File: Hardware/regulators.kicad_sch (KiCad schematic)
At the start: 17 parts, among them J24 DG301-5-0-02P-12-00AH, J25 DG301-5-0-04P-12-00AH, U17 L7812, U19 TLV70033_SOT23-5, U20 TLV73333PDBV

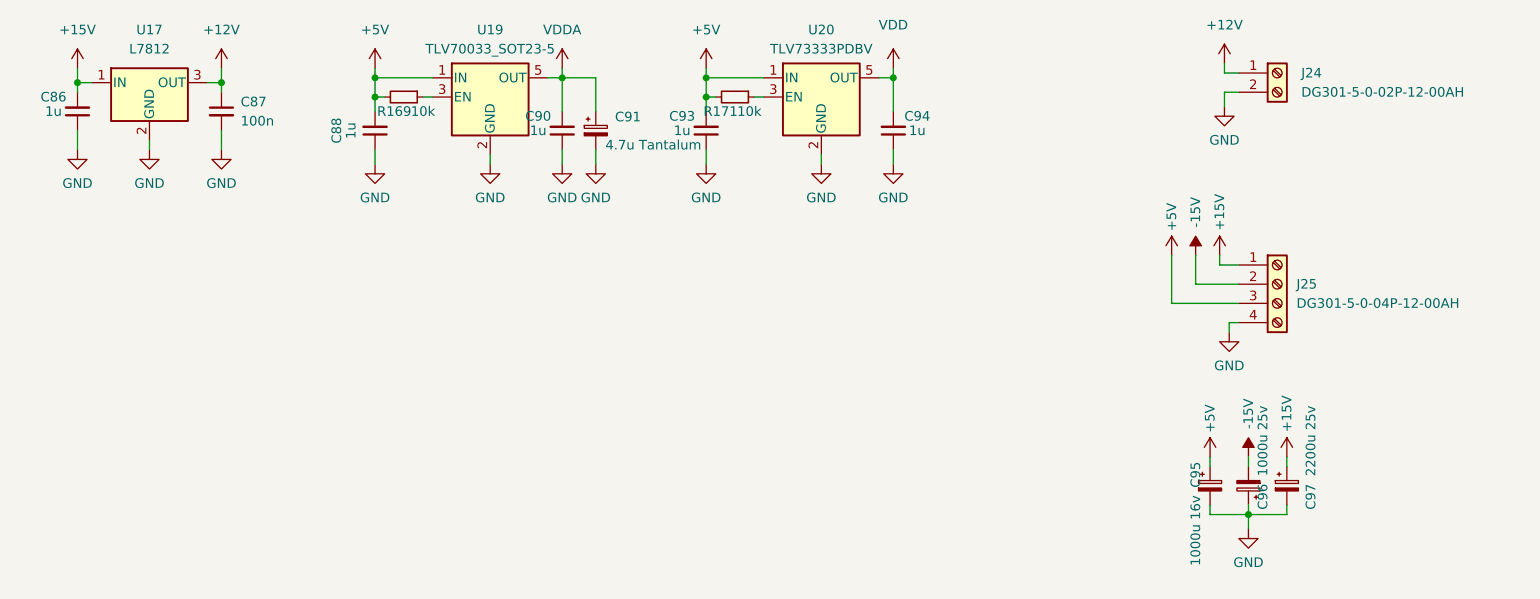
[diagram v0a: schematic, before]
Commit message: Few coonector footprint modifications and silkscreen additions to them.
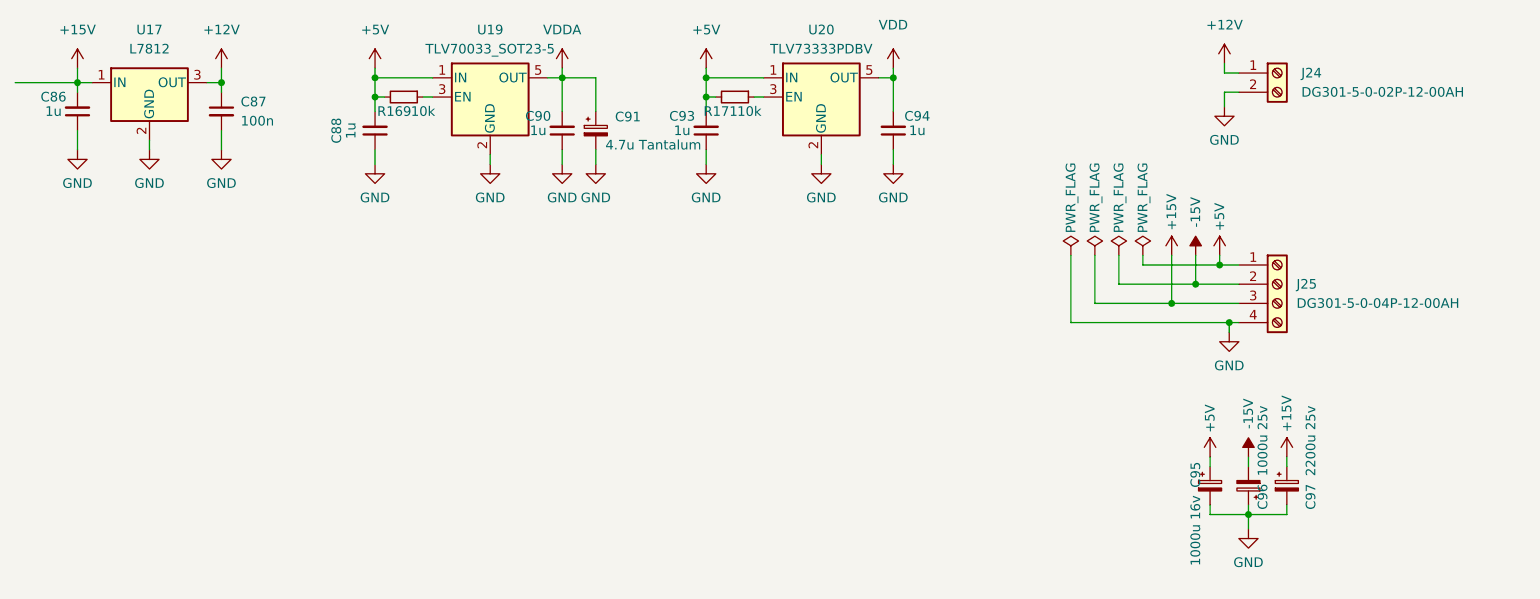
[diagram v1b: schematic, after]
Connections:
- net +15V: now also J25.3 (Pin_3); no longer J25.1 (Pin_1)
- net +5V: now also J25.1 (Pin_1); no longer J25.3 (Pin_3)
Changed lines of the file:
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@@
 (kicad_sch (version 20211123) (generator eeschema)
   (paper "A4")
+  (junction (at 234.95 97.79) (diameter 0) (color 0 0 0 0)
+  )
+  (junction (at 238.125 95.25) (diameter 0) (color 0 0 0 0)
+  )
   (junction (at 245.11 125.73) (diameter 0) (color 0 0 0 0)
   )
+  (junction (at 242.57 100.33) (diameter 0) (color 0 0 0 0)
+  )
   (junction (at 173.355 70.485) (diameter 0) (color 0 0 0 0)
   )
@@
   (junction (at 173.355 67.945) (diameter 0) (color 0 0 0 0)
   )
+  (junction (at 241.3 92.71) (diameter 0) (color 0 0 0 0)
+  )
   (junction (at 109.22 68.58) (diameter 0) (color 0 0 0 0)
   )
@@
     (stroke (width 0) (type default) (color 0 0 0 0))
   )
+  (wire (pts (xy 221.615 91.44) (xy 221.615 100.33))
+    (stroke (width 0) (type default) (color 0 0 0 0))
+  )
   (wire (pts (xy 158.75 72.39) (xy 158.75 67.945))
     (stroke (width 0) (type default) (color 0 0 0 0))
@@
     (stroke (width 0) (type default) (color 0 0 0 0))
   )
+  (wire (pts (xy 81.915 68.58) (xy 90.17 68.58))
+    (stroke (width 0) (type default) (color 0 0 0 0))
+  )
   (wire (pts (xy 173.355 77.47) (xy 173.355 79.375))
     (stroke (width 0) (type default) (color 0 0 0 0))
@@
     (stroke (width 0) (type default) (color 0 0 0 0))
   )
+  (wire (pts (xy 221.615 100.33) (xy 242.57 100.33))
+    (stroke (width 0) (type default) (color 0 0 0 0))
+  )
   (wire (pts (xy 245.11 118.11) (xy 245.11 119.38))
     (stroke (width 0) (type default) (color 0 0 0 0))
@@
     (stroke (width 0) (type default) (color 0 0 0 0))
   )
+  (wire (pts (xy 227.965 91.44) (xy 227.965 95.25))
+    (stroke (width 0) (type default) (color 0 0 0 0))
+  )
   (wire (pts (xy 241.3 92.71) (xy 243.84 92.71))
     (stroke (width 0) (type default) (color 0 0 0 0))
@@
     (stroke (width 0) (type default) (color 0 0 0 0))
   )
+  (wire (pts (xy 224.79 97.79) (xy 234.95 97.79))
+    (stroke (width 0) (type default) (color 0 0 0 0))
+  )
   (wire (pts (xy 109.22 68.58) (xy 109.22 66.675))
     (stroke (width 0) (type default) (color 0 0 0 0))
@@
     (stroke (width 0) (type default) (color 0 0 0 0))
   )
+  (wire (pts (xy 231.14 91.44) (xy 231.14 92.71))
+    (stroke (width 0) (type default) (color 0 0 0 0))
+  )
+  (wire (pts (xy 224.79 91.44) (xy 224.79 97.79))
+    (stroke (width 0) (type default) (color 0 0 0 0))
+  )
   (wire (pts (xy 245.11 125.73) (xy 250.19 125.73))
     (stroke (width 0) (type default) (color 0 0 0 0))
@@
     (stroke (width 0) (type default) (color 0 0 0 0))
   )
+  (wire (pts (xy 231.14 92.71) (xy 241.3 92.71))
+    (stroke (width 0) (type default) (color 0 0 0 0))
+  )
   (wire (pts (xy 241.935 69.85) (xy 241.935 71.755))
     (stroke (width 0) (type default) (color 0 0 0 0))
@@
   )
   (wire (pts (xy 250.19 125.73) (xy 250.19 124.46))
+    (stroke (width 0) (type default) (color 0 0 0 0))
+  )
+  (wire (pts (xy 227.965 95.25) (xy 238.125 95.25))
     (stroke (width 0) (type default) (color 0 0 0 0))
   )
@@
     (pin "2")
   )
-  (symbol (lib_id "power:+15V") (at 241.3 91.44 0) (unit 1)
-    (in_bom yes) (on_board yes)
-    (property "Reference" "#PWR0175" (id 0) (at 241.3 95.25 0)
-      (effects (font (size 1.27 1.27)) hide)
-    )
-    (property "Value" "+15V" (id 1) (at 241.3 85.725 90))
-    (property "Footprint" "" (id 2) (at 241.3 91.44 0)
-      (effects (font (size 1.27 1.27)) hide)
-    )
-    (property "Datasheet" "" (id 3) (at 241.3 91.44 0)
+  (symbol (lib_id "power:PWR_FLAG") (at 224.79 91.44 0) (unit 1)
+    (in_bom yes) (on_board yes)
+    (property "Reference" "#FLG0104" (id 0) (at 224.79 89.535 0)
+      (effects (font (size 1.27 1.27)) hide)
+    )
+    (property "Value" "PWR_FLAG" (id 1) (at 224.79 83.82 90))
+    (property "Footprint" "" (id 2) (at 224.79 91.44 0)
+      (effects (font (size 1.27 1.27)) hide)
+    )
+    (property "Datasheet" "~" (id 3) (at 224.79 91.44 0)
+      (effects (font (size 1.27 1.27)) hide)
+    )
+    (pin "1")
+  )
+  (symbol (lib_id "power:+15V") (at 234.95 91.44 0) (unit 1)
+    (in_bom yes) (on_board yes)
+    (property "Reference" "#PWR0175" (id 0) (at 234.95 95.25 0)
+      (effects (font (size 1.27 1.27)) hide)
+    )
+    (property "Value" "+15V" (id 1) (at 234.95 85.725 90))
+    (property "Footprint" "" (id 2) (at 234.95 91.44 0)
+      (effects (font (size 1.27 1.27)) hide)
+    )
+    (property "Datasheet" "" (id 3) (at 234.95 91.44 0)
       (effects (font (size 1.27 1.27)) hide)
     )
@@
     (pin "2")
   )
+  (symbol (lib_id "power:PWR_FLAG") (at 231.14 91.44 0) (unit 1)
+    (in_bom yes) (on_board yes)
+    (property "Reference" "#FLG0103" (id 0) (at 231.14 89.535 0)
+      (effects (font (size 1.27 1.27)) hide)
+    )
+    (property "Value" "PWR_FLAG" (id 1) (at 231.14 83.82 90))
+    (property "Footprint" "" (id 2) (at 231.14 91.44 0)
+      (effects (font (size 1.27 1.27)) hide)
+    )
+    (property "Datasheet" "~" (id 3) (at 231.14 91.44 0)
+      (effects (font (size 1.27 1.27)) hide)
+    )
+    (pin "1")
+  )
   (symbol (lib_id "Device:R_Small") (at 133.35 70.485 270) (unit 1)
     (in_bom yes) (on_board yes)
@@
     (pin "2")
   )
+  (symbol (lib_id "power:PWR_FLAG") (at 227.965 91.44 0) (unit 1)
+    (in_bom yes) (on_board yes)
+    (property "Reference" "#FLG0101" (id 0) (at 227.965 89.535 0)
+      (effects (font (size 1.27 1.27)) hide)
+    )
+    (property "Value" "PWR_FLAG" (id 1) (at 227.965 83.82 90))
+    (property "Footprint" "" (id 2) (at 227.965 91.44 0)
+      (effects (font (size 1.27 1.27)) hide)
+    )
+    (property "Datasheet" "~" (id 3) (at 227.965 91.44 0)
+      (effects (font (size 1.27 1.27)) hide)
+    )
+    (pin "1")
+  )
   (symbol (lib_id "power:+5V") (at 173.355 66.675 0) (unit 1)
     (in_bom yes) (on_board yes) (fields_autoplaced)
@@
     (pin "2")
   )
-  (symbol (lib_id "power:+5V") (at 234.95 91.44 0) (unit 1)
-    (in_bom yes) (on_board yes)
-    (property "Reference" "#PWR0172" (id 0) (at 234.95 95.25 0)
-      (effects (font (size 1.27 1.27)) hide)
-    )
-    (property "Value" "+5V" (id 1) (at 234.95 86.36 90))
-    (property "Footprint" "" (id 2) (at 234.95 91.44 0)
-      (effects (font (size 1.27 1.27)) hide)
-    )
-    (property "Datasheet" "" (id 3) (at 234.95 91.44 0)
+  (symbol (lib_id "power:+5V") (at 241.3 91.44 0) (unit 1)
+    (in_bom yes) (on_board yes)
+    (property "Reference" "#PWR0172" (id 0) (at 241.3 95.25 0)
+      (effects (font (size 1.27 1.27)) hide)
+    )
+    (property "Value" "+5V" (id 1) (at 241.3 86.36 90))
+    (property "Footprint" "" (id 2) (at 241.3 91.44 0)
+      (effects (font (size 1.27 1.27)) hide)
+    )
+    (property "Datasheet" "" (id 3) (at 241.3 91.44 0)
       (effects (font (size 1.27 1.27)) hide)
     )
@@
     (pin "2")
   )
+  (symbol (lib_id "power:PWR_FLAG") (at 221.615 91.44 0) (unit 1)
+    (in_bom yes) (on_board yes)
+    (property "Reference" "#FLG0105" (id 0) (at 221.615 89.535 0)
+      (effects (font (size 1.27 1.27)) hide)
+    )
+    (property "Value" "PWR_FLAG" (id 1) (at 221.615 83.82 90))
+    (property "Footprint" "" (id 2) (at 221.615 91.44 0)
+      (effects (font (size 1.27 1.27)) hide)
+    )
+    (property "Datasheet" "~" (id 3) (at 221.615 91.44 0)
+      (effects (font (size 1.27 1.27)) hide)
+    )
+    (pin "1")
+  )
   (symbol (lib_id "power:GND") (at 198.12 79.375 0) (unit 1)
